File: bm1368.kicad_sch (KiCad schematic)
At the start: 50 parts, among them U5 MCP1824T-1202E/OT, U6 MCP1824T-0802E, U7 25MHz, U8 BM1368_mode1, U9 SN74AVC4T774

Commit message: DK partnumber update on the 330uF cap
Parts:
- C43: DK 490-GRM32ER60G337ME05KTR-ND -> 490-GRM32ER60G337ME05KCT-ND
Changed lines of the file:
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@@
 			)
 		)
-		(property "DK" "490-GRM32ER60G337ME05KTR-ND"
+		(property "DK" "490-GRM32ER60G337ME05KCT-ND"
 			(at 147.32 57.15 0)
 			(effects

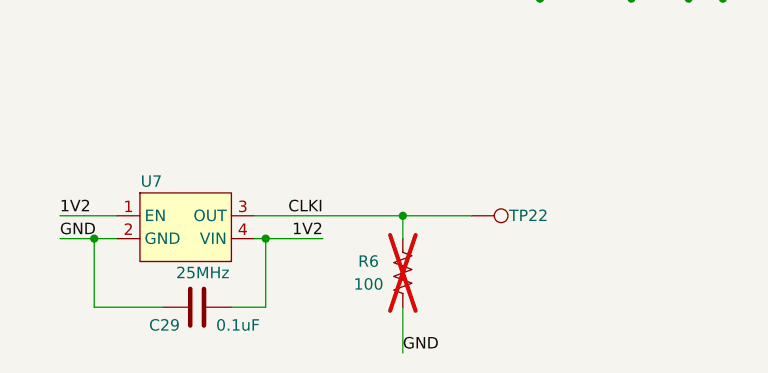
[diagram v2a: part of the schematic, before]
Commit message: moved C43 (and some other stuff) out of the way of the heatsink for #168
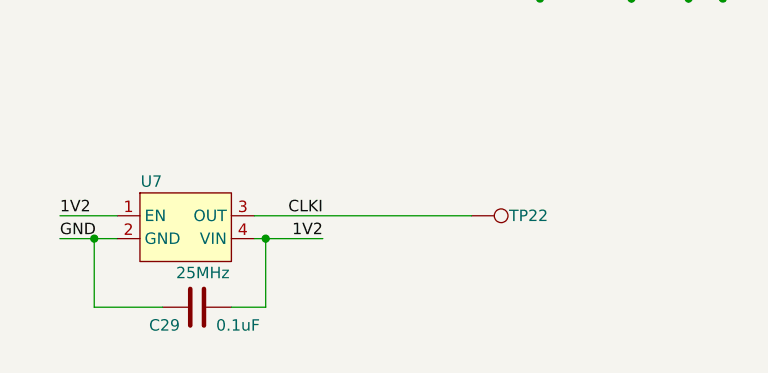
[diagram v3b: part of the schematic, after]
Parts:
- removed R6: 100, Resistor_SMD:R_0402_1005Metric, symbol Device:R_US
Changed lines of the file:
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@@
 	)
 	(junction
-		(at 66.04 170.18)
-		(diameter 0)
-		(color 0 0 0 0)
-	)
-	(junction
 		(at 170.18 146.05)
 		(diameter 0)
@@
 	(wire
 		(pts
-			(xy 66.04 180.34) (xy 66.04 185.42)
-		)
-		(stroke
-			(width 0)
-			(type default)
-		)
-	)
-	(wire
-		(pts
 			(xy 87.63 85.09) (xy 88.9 85.09)
 		)
@@
 	(wire
 		(pts
-			(xy 66.04 170.18) (xy 66.04 172.72)
-		)
-		(stroke
-			(width 0)
-			(type default)
-		)
-	)
-	(wire
-		(pts
 			(xy 158.75 116.84) (xy 176.53 116.84)
 		)
@@
 	(wire
 		(pts
-			(xy 66.04 170.18) (xy 73.66 170.18)
-		)
-		(stroke
-			(width 0)
-			(type default)
-		)
-	)
-	(wire
-		(pts
 			(xy 125.73 50.8) (xy 135.89 50.8)
 		)
@@
 	(wire
 		(pts
-			(xy 49.53 170.18) (xy 66.04 170.18)
+			(xy 49.53 170.18) (xy 73.66 170.18)
 		)
 		(stroke
@@
 		)
 	)
-	(label "GND"
-		(at 66.04 185.42 0)
-		(fields_autoplaced yes)
-		(effects
-			(font
-				(size 1.27 1.27)
-			)
-			(justify left bottom)
-		)
-	)
 	(label "BO"
 		(at 215.9 114.3 0)
@@
 					(unit 1)
 				)
-			)
-		)
-	)
-	(symbol
-		(lib_id "Device:R_US")
-		(at 66.04 176.53 180)
-		(unit 1)
-		(exclude_from_sim no)
-		(in_bom no)
-		(on_board yes)
-		(dnp yes)
-		(property "Reference" "R6"
-			(at 62.23 175.26 0)
-			(effects
-				(font
-					(size 1.27 1.27)
-				)
-			)
-		)
-		(property "Value" "100"
-			(at 62.23 177.8 0)
-			(effects
-				(font
-					(size 1.27 1.27)
-				)
-			)
-		)
-		(property "Footprint" "Resistor_SMD:R_0402_1005Metric"
-			(at 65.024 176.276 90)
-			(effects
-				(font
-					(size 1.27 1.27)
-				)
-				(hide yes)
-			)
-		)
-		(property "Datasheet" "~"
-			(at 66.04 176.53 0)
-			(effects
-				(font
-					(size 1.27 1.27)
-				)
-				(hide yes)
-			)
-		)
-		(property "Description" ""
-			(at 66.04 176.53 0)
-			(effects
-				(font
-					(size 1.27 1.27)
-				)
-				(hide yes)
-			)
-		)
-		(property "DK" "311-100LRCT-ND"
-			(at 66.04 176.53 0)
-			(effects
-				(font
-					(size 1.27 1.27)
-				)
-				(hide yes)
-			)
-		)
-		(property "PARTNO" "RC0402FR-07100RL"
-			(at 66.04 176.53 0)
-			(effects
-				(font
-					(size 1.27 1.27)
-				)
-				(hide yes)
-			)
-		)
-		(pin "1"
-		)
-		(pin "2"
-		)
-		(instances
-			(project "bm1397"
-				(path "/5ffa02c9-1f90-4b06-abee-1fc0c47a0c88"
-					(reference "R6")
-					(unit 1)
-				)
-			)
-			(project "bitaxeSupra"
-				(path "/e63e39d7-6ac0-4ffd-8aa3-1841a4541b55/4cf9c075-d009-4c35-9949-adda70ae20c7"
-					(reference "R20")
-					(unit 1)
-				)

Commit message: caps, back plane
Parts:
- C43: footprint Capacitor_SMD:C_1210_3225Metric -> Capacitor_SMD:C_1206_3216Metric
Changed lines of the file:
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@@
 			)
 		)
-		(property "Footprint" "Capacitor_SMD:C_1210_3225Metric"
+		(property "Footprint" "Capacitor_SMD:C_1206_3216Metric"
 			(at 148.2852 60.96 0)
 			(effects

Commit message: normalized 0.1uF capacitor part numbers
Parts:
- C29, C37, C38, C47, C49: DK 1292-1639-1-ND -> 1276-1234-1-ND; PARTNO 0402X104K100CT -> CL05A104KO5NNNC
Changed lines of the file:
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@@
 			)
 		)
-		(property "DK" "1292-1639-1-ND"
+		(property "DK" "1276-1234-1-ND"
 			(at 115.57 57.15 0)
 			(effects
@@
 			)
 		)
-		(property "PARTNO" "0402X104K100CT"
+		(property "PARTNO" "CL05A104KO5NNNC"
 			(at 115.57 57.15 0)
 			(effects
@@
 			)
 		)
-		(property "DK" "1292-1639-1-ND"
+		(property "DK" "1276-1234-1-ND"
 			(at 43.18 180.34 0)
 			(effects
@@
 			)
 		)
-		(property "PARTNO" "0402X104K100CT"
+		(property "PARTNO" "CL05A104KO5NNNC"
 			(at 43.18 180.34 0)
 			(effects
@@
 			)
 		)
-		(property "DK" "1292-1639-1-ND"
+		(property "DK" "1276-1234-1-ND"
 			(at 105.41 57.15 0)
 			(effects
@@
 			)
 		)
-		(property "PARTNO" "0402X104K100CT"
+		(property "PARTNO" "CL05A104KO5NNNC"
 			(at 105.41 57.15 0)
 			(effects
@@
 			)
 		)
-		(property "DK" "1292-1639-1-ND"
+		(property "DK" "1276-1234-1-ND"
 			(at 242.57 39.37 0)
 			(effects
@@
 			)
 		)
-		(property "PARTNO" "0402X104K100CT"
+		(property "PARTNO" "CL05A104KO5NNNC"
 			(at 242.57 39.37 0)
 			(effects
@@
 			)
 		)
-		(property "DK" "1292-1639-1-ND"
+		(property "DK" "1276-1234-1-ND"
 			(at 173.99 39.37 0)
 			(effects
@@
 			)
 		)
-		(property "PARTNO" "0402X104K100CT"
+		(property "PARTNO" "CL05A104KO5NNNC"
 			(at 173.99 39.37 0)
 			(effects

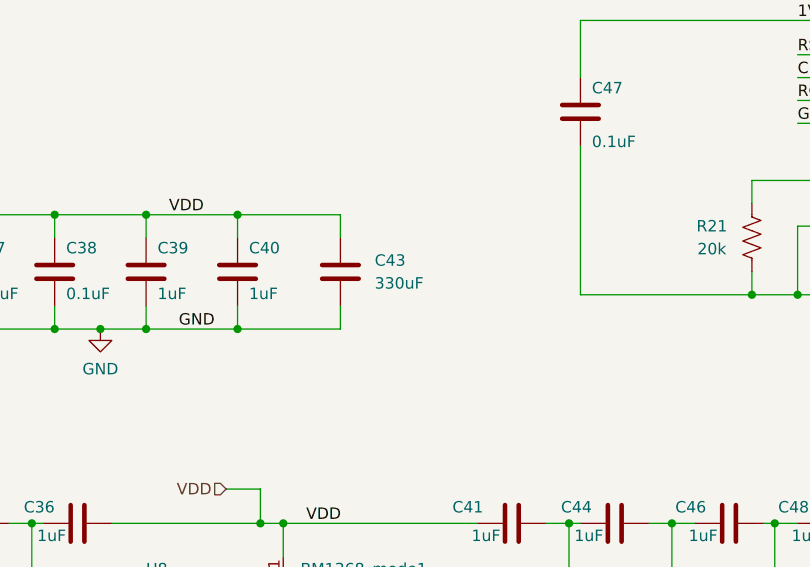
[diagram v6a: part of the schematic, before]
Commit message: change C43 to 100uF
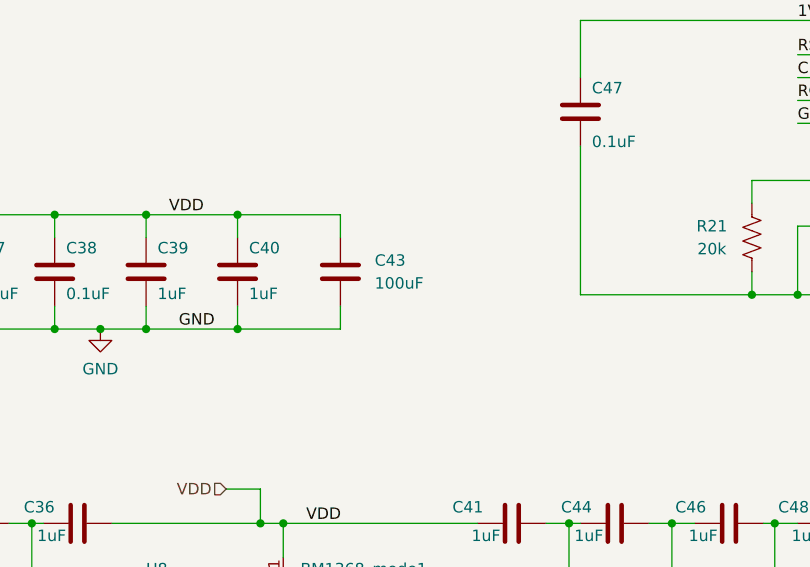
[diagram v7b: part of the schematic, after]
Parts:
- C43: value 330uF -> 100uF; DK 490-GRM32ER60G337ME05KCT-ND -> 1276-1782-2-ND; PARTNO GRM32ER60G337ME05K -> CL31A107MQHNNNE
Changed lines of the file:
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@@
 			)
 		)
-		(property "Value" "330uF"
+		(property "Value" "100uF"
 			(at 151.13 58.4199 0)
 			(effects
@@
 			)
 		)
-		(property "DK" "490-GRM32ER60G337ME05KCT-ND"
+		(property "DK" "1276-1782-2-ND"
 			(at 147.32 57.15 0)
 			(effects
@@
 			)
 		)
-		(property "PARTNO" "GRM32ER60G337ME05K"
+		(property "PARTNO" "CL31A107MQHNNNE"
 			(at 147.32 57.15 0)
 			(effects

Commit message: fixed 25MHz oscillator package name and part number in project and BOM
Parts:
- U7: footprint bitaxe:O 25,0-JO32-B-1V3-1-T1-LF -> bitaxe:SMD3225-4P
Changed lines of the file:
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@@
 			)
 		)
-		(property "Footprint" "bitaxe:O 25,0-JO32-B-1V3-1-T1-LF"
+		(property "Footprint" "bitaxe:SMD3225-4P"
 			(at 40.64 172.72 0)
 			(effects
